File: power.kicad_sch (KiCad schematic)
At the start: 39 parts, among them J5 Molex_Nano-Fit_1x2_105309-1202, Q1 AO3401A, Q5 BCM857BS-7-F, Q6 SSM3J332R, SW1 SW_EG1218, U4 AP62301_TSOT, U6 MCP1700T-3302E_TT

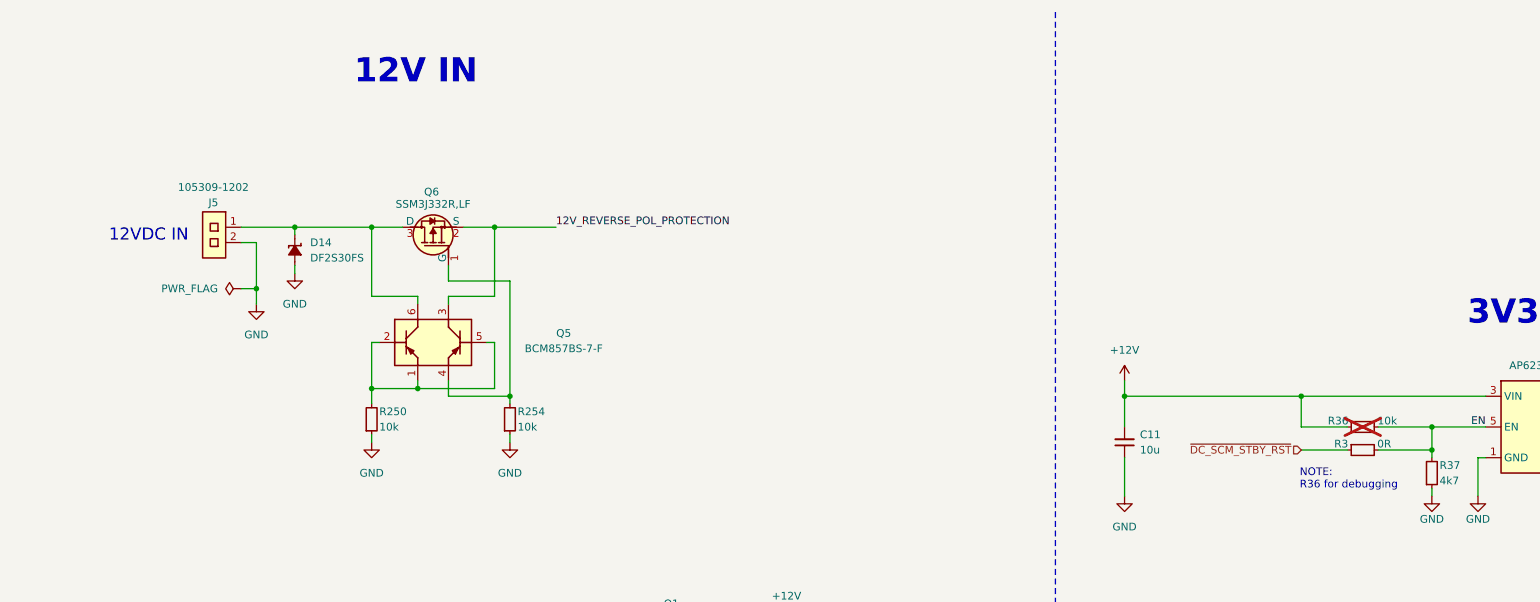
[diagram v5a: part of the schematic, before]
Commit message: [#93949] Align items to grid, change TP for UART
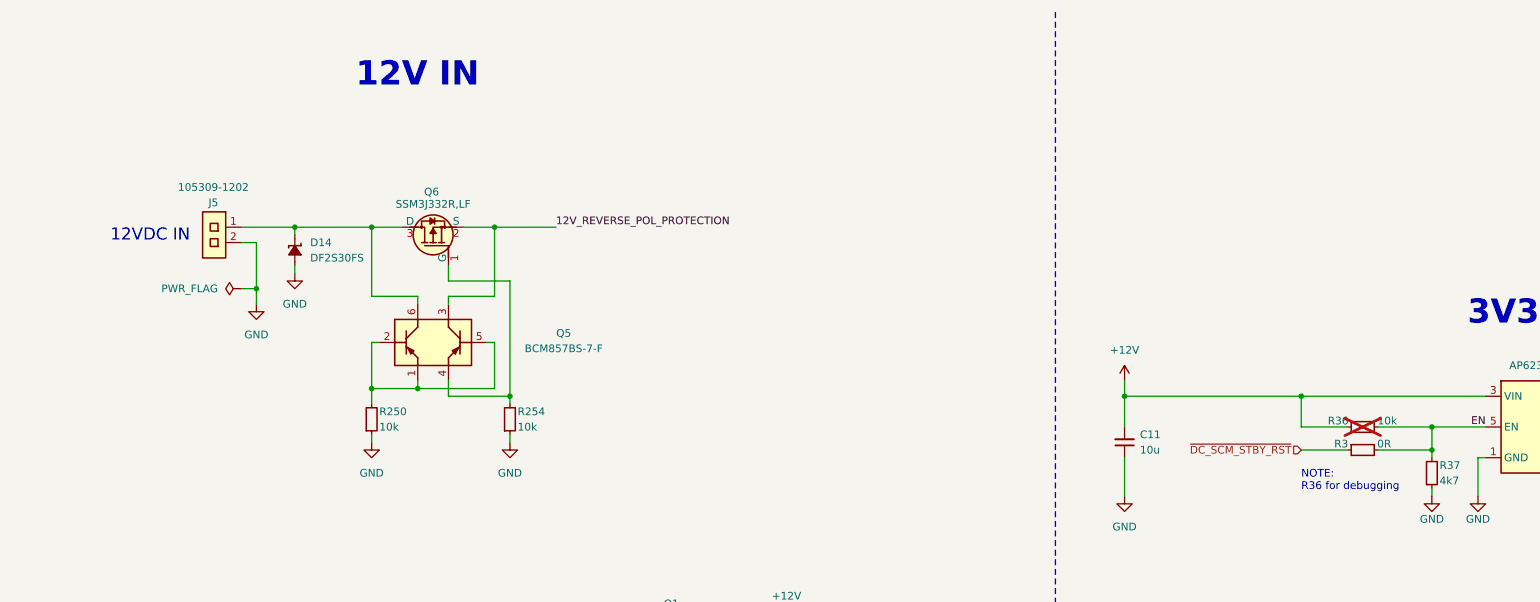
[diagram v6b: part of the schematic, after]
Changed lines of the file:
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@@
 	(text "NOTE:\nR36 for debugging\n"
 		(exclude_from_sim no)
-		(at 249.936 89.916 0)
+		(at 250.19 90.17 0)
 		(effects
 			(font
@@
 	(text "12VDC IN"
 		(exclude_from_sim no)
-		(at 53.086 50.8 0)
+		(at 53.34 50.8 0)
 		(effects
 			(font
@@
 	(text "12V IN"
 		(exclude_from_sim no)
-		(at 114.046 24.892 0)
+		(at 114.3 25.4 0)
 		(effects
 			(font

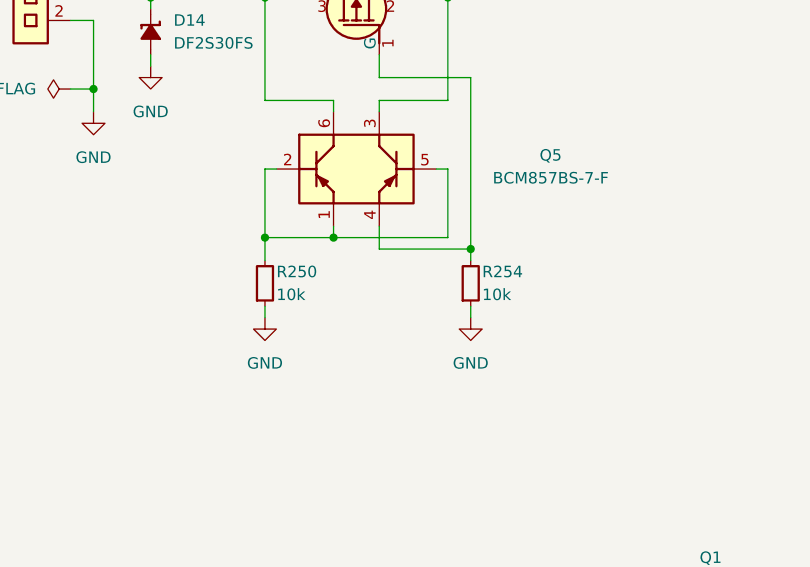
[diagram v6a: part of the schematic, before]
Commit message: [#93949] Change reverse polarity protection resistor references
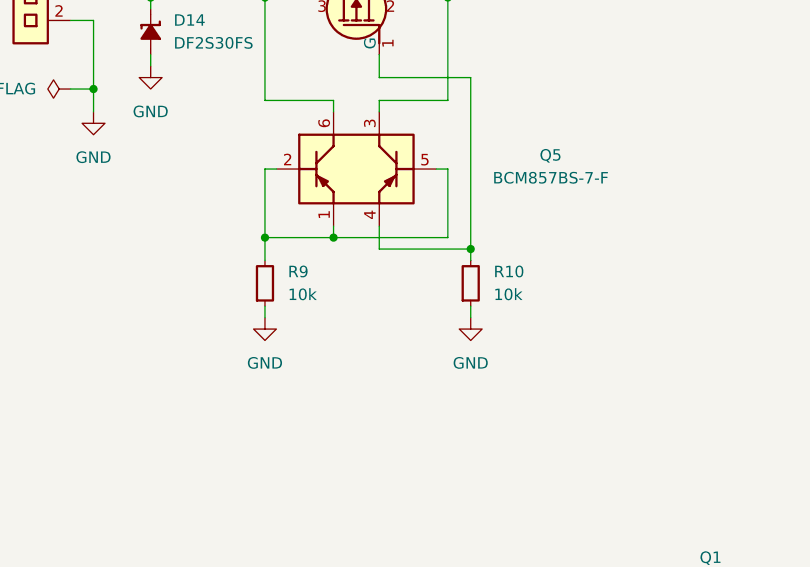
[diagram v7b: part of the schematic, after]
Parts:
- removed R250, R254: R_10k_0402, antmicro-footprints:R_0402_1005Metric, symbol antmicroResistors0402:R_10k_0402
- added R10, R9: R_10k_0402, antmicro-footprints:R_0402_1005Metric, symbol antmicroResistors0402:R_10k_0402
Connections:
- net GND: now also R10.1, R9.1
- net at Q5.4, Q6.1 (G): now also R10.2
- net at Q5.1, Q5.2, Q5.5: now also R9.2
